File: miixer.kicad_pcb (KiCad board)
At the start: 2 copper layers, 60 x 30 mm, 8 parts, among them J1 USB_C_Receptacle_USB2.0_16P, U1 ESP32-C3-WROOM-02, U3 USBLC6-2SC6

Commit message: Update
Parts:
- added VR1: PTL60-15G1-103B2, 00_Luc:PTL6015G1103B2, F.Cu at (38.6, 110.0)
- added VR2: PTL60-15G1-103B2, 00_Luc:PTL6015G1103B2, F.Cu at (50.3, 110.0)
- added VR3: PTL60-15G1-103B2, 00_Luc:PTL6015G1103B2, F.Cu at (61.9, 110.0)
- added VR4: PTL60-15G1-103B2, 00_Luc:PTL6015G1103B2, F.Cu at (73.4, 110.0)
- R4, U1: moved to B.Cu
- moved R5 36.3 mm to (103.2, 32.5)
- moved J1 35.2 mm to (117.8, 37.0)
- moved R1 35.2 mm to (110.0, 37.7)
- moved R2 35.2 mm to (110.0, 35.9)
- moved U3 35.2 mm to (103.3, 36.7)
- moved R6 34.6 mm to (110.0, 32.5)
- moved R4 24.7 mm to (32.5, 44.2), turned to 180 degrees
- moved U1 19.3 mm to (37.7, 55.2), turned to -90 degrees
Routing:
- net /MCU/USB_D+: track 30.9 -> 0.97 mm
- net VBUS: track 2.83 -> 0.00 mm
- net +3.3V: track 0.00 -> 2.27 mm
- net /MCU/ENABLE: track 0.00 -> 2.25 mm
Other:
- board size 60 x 30 mm -> 90 x 90 mm

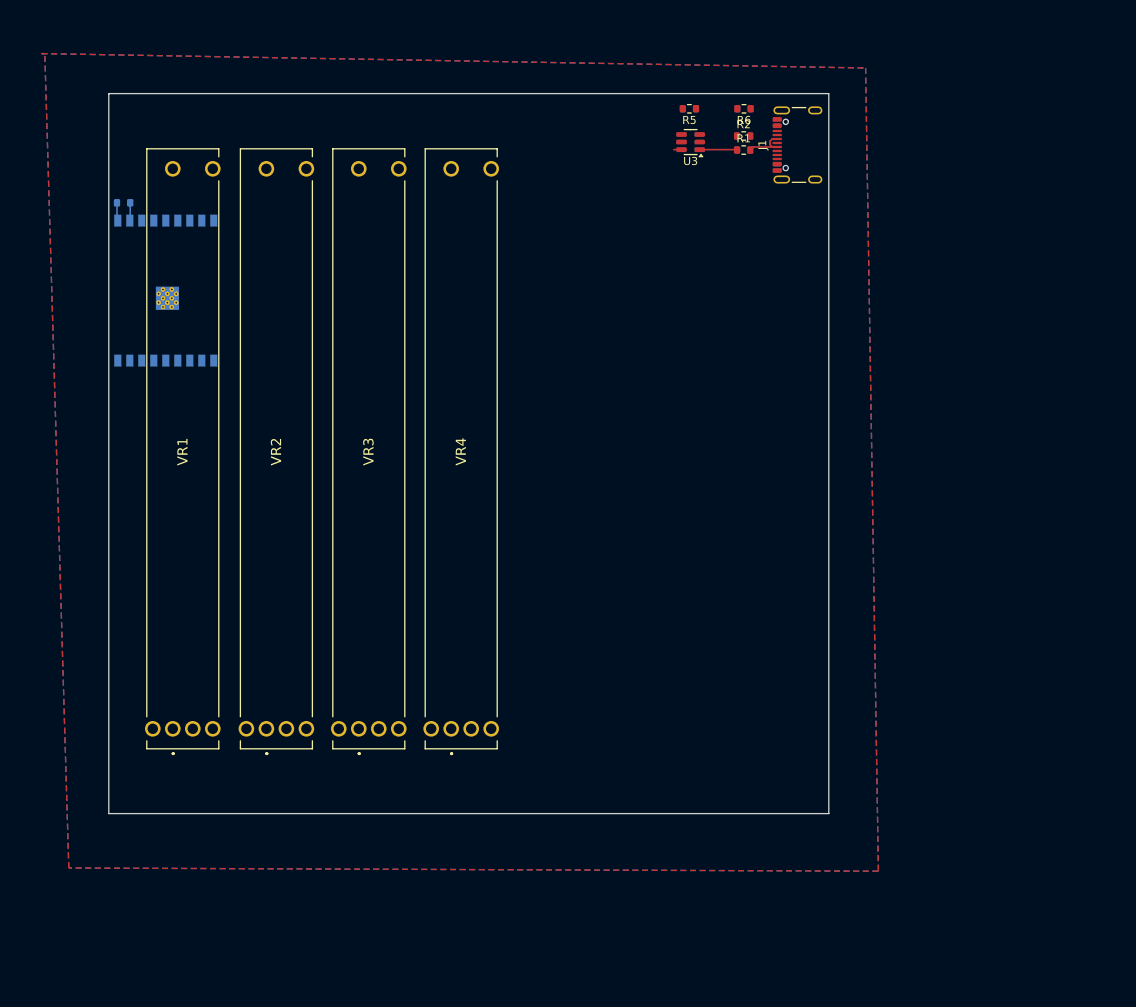
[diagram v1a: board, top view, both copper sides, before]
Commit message: Introduce buttons and update pcb layout
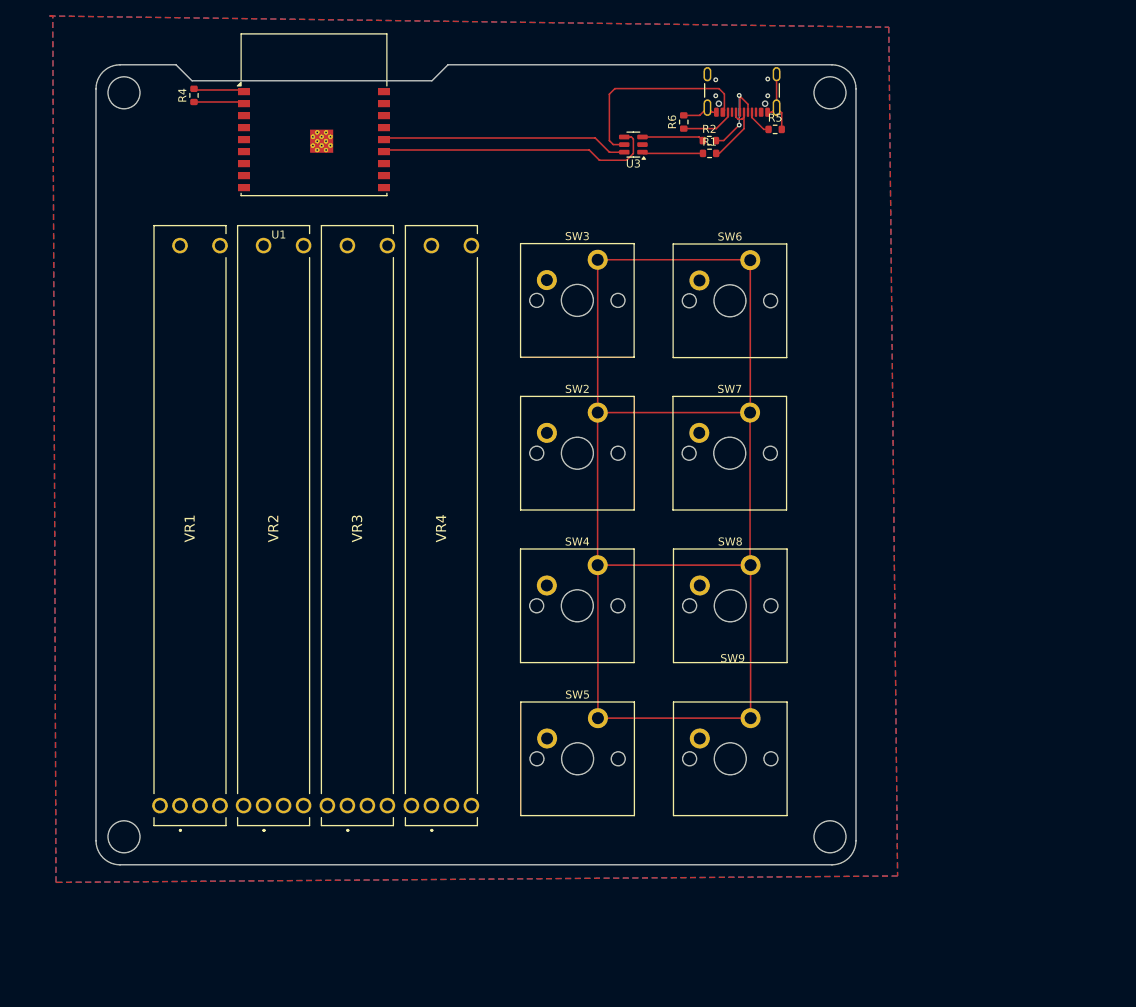
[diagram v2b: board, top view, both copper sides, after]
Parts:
- added SW2: SW_SPST, PCM_Switch_Keyboard_Cherry_MX:SW_Cherry_MX_PCB_1.00u, F.Cu at (89.2, 75.5)
- added SW3: SW_SPST, PCM_Switch_Keyboard_Cherry_MX:SW_Cherry_MX_PCB_1.00u, F.Cu at (89.2, 56.5)
- added SW4: SW_SPST, PCM_Switch_Keyboard_Cherry_MX:SW_Cherry_MX_PCB_1.00u, F.Cu at (89.2, 94.6)
- added SW5: SW_SPST, PCM_Switch_Keyboard_Cherry_MX:SW_Cherry_MX_PCB_1.00u, F.Cu at (89.2, 113.8)
- added SW6: SW_SPST, PCM_Switch_Keyboard_Cherry_MX:SW_Cherry_MX_PCB_1.00u, F.Cu at (108.2, 56.5)
- added SW7: SW_SPST, PCM_Switch_Keyboard_Cherry_MX:SW_Cherry_MX_PCB_1.00u, F.Cu at (108.2, 75.5)
- added SW8: SW_SPST, PCM_Switch_Keyboard_Cherry_MX:SW_Cherry_MX_PCB_1.00u, F.Cu at (108.3, 94.6)
- added SW9: SW_SPST, PCM_Switch_Keyboard_Cherry_MX:SW_Cherry_MX_PCB_1.00u, F.Cu at (108.3, 113.8)
- R4, U1: moved to F.Cu
- moved U1 26.4 mm to (56.2, 36.4), turned to 0 degrees
- moved R4 16.1 mm to (41.2, 30.8), turned to 90 degrees
- moved J1 11.2 mm to (109.8, 29.2), turned to 180 degrees
- moved R5 11.0 mm to (113.9, 35.1), turned to 0 degrees
- moved VR4 9.91 mm to (70.9, 119.6)
- moved VR3 9.71 mm to (60.4, 119.6)
- moved VR1 9.64 mm to (39.5, 119.6)
- moved VR2 9.61 mm to (50.0, 119.6)
- moved R6 7.71 mm to (102.5, 34.1), turned to 90 degrees
- moved U3 7.16 mm to (96.2, 37.0)
- moved R2 4.33 mm to (105.7, 36.5)
- moved R1 4.29 mm to (105.7, 38.1)
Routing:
- net GND: track 0.00 -> 204.2 mm, vias 0 -> 4
- net /MCU/USB_D-: track 0.00 -> 35.1 mm
- net /MCU/USB_D+: track 0.97 -> 30.8 mm
- net VBUS: track 0.00 -> 25.2 mm
- net /USB/USB_D-_RAW: track 0.00 -> 12.1 mm, vias 0 -> 2
- net /USB/USB_DN: track 0.00 -> 7.72 mm
- net /USB/CC2: track 0.00 -> 6.71 mm
- net +3.3V: track 2.27 -> 6.30 mm
- net /MCU/ENABLE: track 2.25 -> 6.24 mm
- net /USB/CC1: track 0.00 -> 3.35 mm
- net /USB/USB_D+_RAW: track 5.96 -> 9.26 mm
- net /USB/USB_DP: track 4.70 -> 7.62 mm
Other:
- board size 90 x 90 mm -> 95 x 100 mm

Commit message: Make square
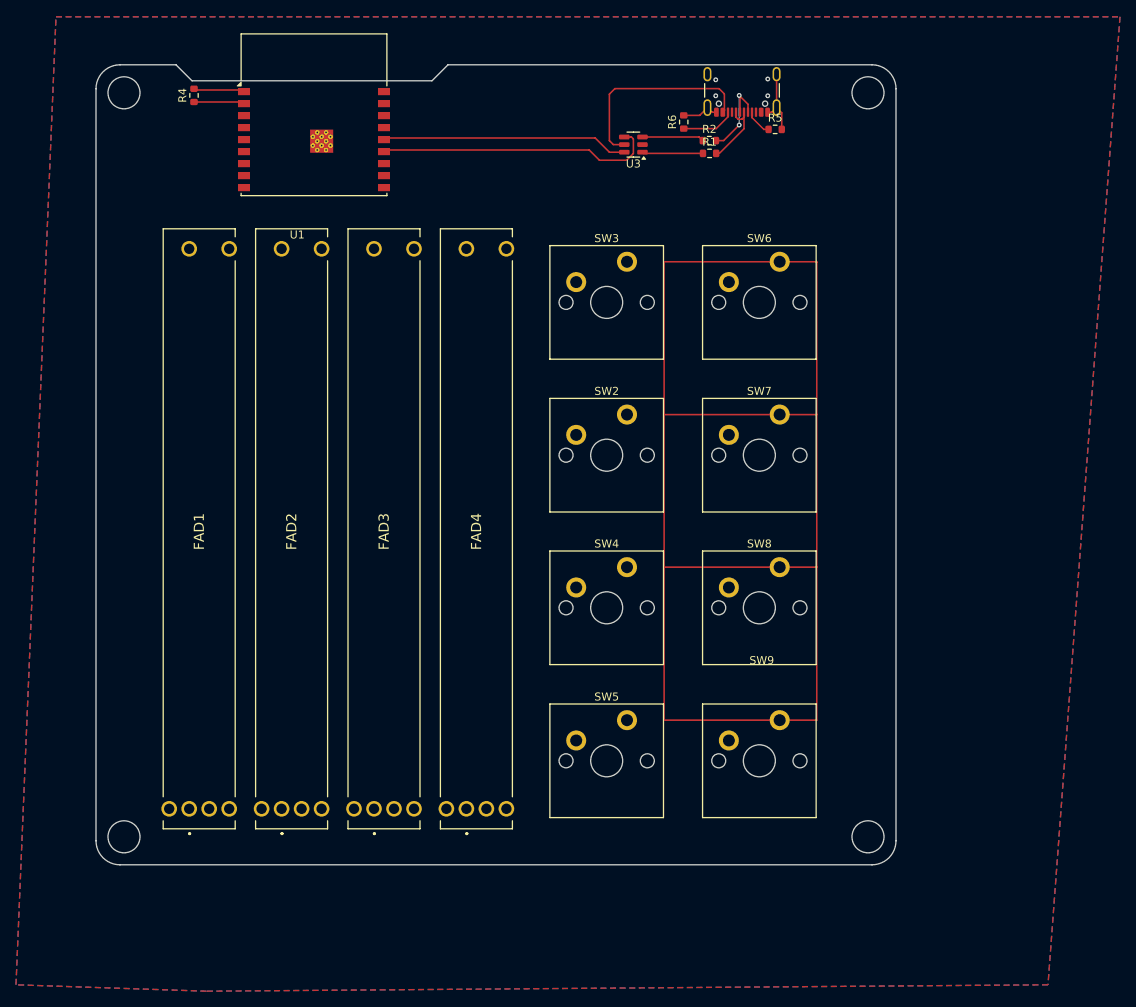
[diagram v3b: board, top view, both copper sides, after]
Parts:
- removed VR1, VR2, VR3, VR4: PTL60-15G1-103B2, 00_Luc:PTL6015G1103B2
- added FAD1: PTL60-15G1-103B2, 00_Luc:PTL6015G1103B2, F.Cu at (40.6, 120.0)
- added FAD2: PTL60-15G1-103B2, 00_Luc:PTL6015G1103B2, F.Cu at (52.2, 120.0)
- added FAD3: PTL60-15G1-103B2, 00_Luc:PTL6015G1103B2, F.Cu at (63.8, 120.0)
- added FAD4: PTL60-15G1-103B2, 00_Luc:PTL6015G1103B2, F.Cu at (75.3, 120.0)
- moved SW7 3.71 mm to (111.9, 75.8)
- moved SW6 3.68 mm to (111.9, 56.7)
- moved SW4 3.68 mm to (92.8, 94.9)
- moved SW3 3.67 mm to (92.8, 56.7)
- moved SW2 3.67 mm to (92.8, 75.8)
- moved SW8 3.64 mm to (111.9, 94.9)
- moved SW9 3.64 mm to (111.9, 114.0)
- moved SW5 3.64 mm to (92.8, 114.0)
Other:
- board size 95 x 100 mm -> 100 x 100 mm

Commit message: Add keys for each fader & update layout
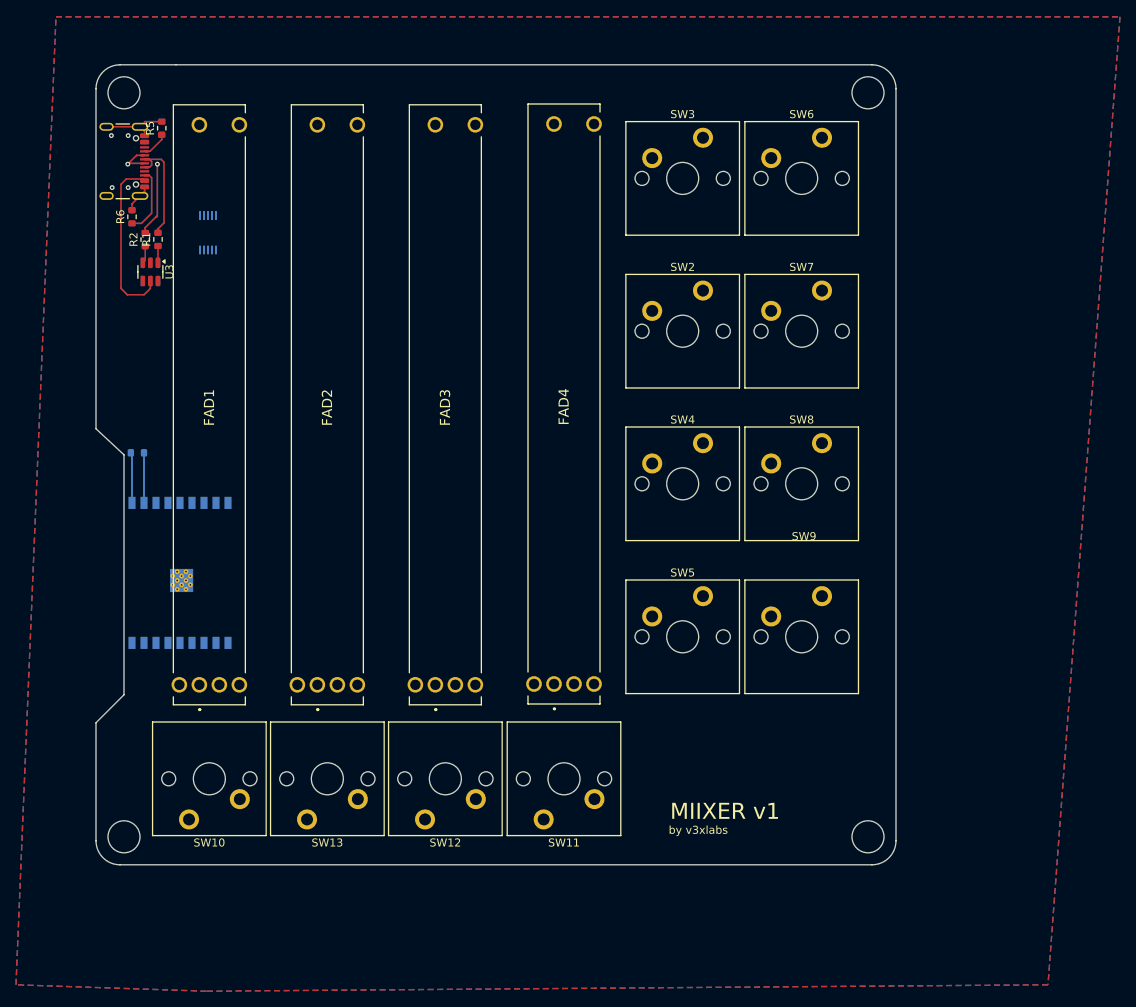
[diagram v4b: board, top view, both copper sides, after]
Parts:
- added SW10: SW_SPST, PCM_Switch_Keyboard_Cherry_MX:SW_Cherry_MX_PCB_1.00u, F.Cu at (43.2, 116.2)
- added SW11: SW_SPST, PCM_Switch_Keyboard_Cherry_MX:SW_Cherry_MX_PCB_1.00u, F.Cu at (87.5, 116.2)
- added SW12: SW_SPST, PCM_Switch_Keyboard_Cherry_MX:SW_Cherry_MX_PCB_1.00u, F.Cu at (72.7, 116.2)
- added SW13: SW_SPST, PCM_Switch_Keyboard_Cherry_MX:SW_Cherry_MX_PCB_1.00u, F.Cu at (57.9, 116.2)
- added U2: ADS1115IDGS, Package_SO:TSSOP-10_3x3mm_P0.5mm, B.Cu at (43.0, 48.0)
- R4, U1: moved to B.Cu
- moved J1 79.0 mm to (31.4, 39.1), turned to -90 degrees
- moved R5 76.7 mm to (37.2, 34.9), turned to 90 degrees
- moved R2 71.6 mm to (35.1, 48.9), turned to 90 degrees
- moved R6 70.0 mm to (33.5, 46.0)
- moved R1 69.8 mm to (36.8, 48.8), turned to 90 degrees
- moved U3 62.4 mm to (35.8, 52.9), turned to -90 degrees
- moved U1 56.7 mm to (39.5, 90.5), turned to -90 degrees
- moved R4 45.2 mm to (34.2, 75.5), turned to 180 degrees
- moved FAD4 19.1 mm to (86.2, 104.4)
- moved SW2 18.2 mm to (102.3, 60.3)
- moved SW3 18.2 mm to (102.3, 41.2)
- moved SW4 18.2 mm to (102.3, 79.4)
- moved SW5 18.2 mm to (102.3, 98.5)
- moved FAD3 17.3 mm to (71.4, 104.5)
- moved SW6 16.4 mm to (117.2, 41.2)
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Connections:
- FAD1 pad 1: unconnected-(FAD1-CCW-Pad1) -> Net-(FAD1-CCW)
- FAD1 pad B1: unconnected-(FAD1-B_(+)-PadB1) -> Net-(FAD1-B_(+))
- FAD1 pad E1: unconnected-(FAD1-E_(-)-PadE1) -> GND
- FAD2 pad 1: unconnected-(FAD2-CCW-Pad1) -> Net-(FAD2-CCW)
- FAD2 pad B1: unconnected-(FAD2-B_(+)-PadB1) -> Net-(FAD2-B_(+))
- FAD2 pad E1: unconnected-(FAD2-E_(-)-PadE1) -> GND
- FAD3 pad 1: unconnected-(FAD3-CCW-Pad1) -> Net-(FAD3-CCW)
- FAD3 pad B1: unconnected-(FAD3-B_(+)-PadB1) -> Net-(FAD3-B_(+))
- FAD3 pad E1: unconnected-(FAD3-E_(-)-PadE1) -> GND
- FAD4 pad 1: unconnected-(FAD4-CCW-Pad1) -> Net-(FAD4-CCW)
- FAD4 pad B1: unconnected-(FAD4-B_(+)-PadB1) -> Net-(FAD4-B_(+))
- FAD4 pad E1: unconnected-(FAD4-E_(-)-PadE1) -> GND
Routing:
- net GND: track 204.2 -> 12.1 mm
- net /MCU/USB_D-: track 35.1 -> 0.00 mm
- net /MCU/USB_D+: track 30.8 -> 0.00 mm
- net /USB/USB_DN: track 7.72 -> 2.20 mm
- net /USB/USB_DP: track 7.62 -> 2.10 mm
- net /USB/USB_D+_RAW: track 9.26 -> 14.1 mm
- net VBUS: track 25.2 -> 21.6 mm
- net /USB/CC2: track 6.71 -> 8.98 mm
- net /USB/USB_D-_RAW: track 12.1 -> 14.0 mm
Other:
- outline, holes or cut-outs redrawn

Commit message: Reorg layout and remove fader keys
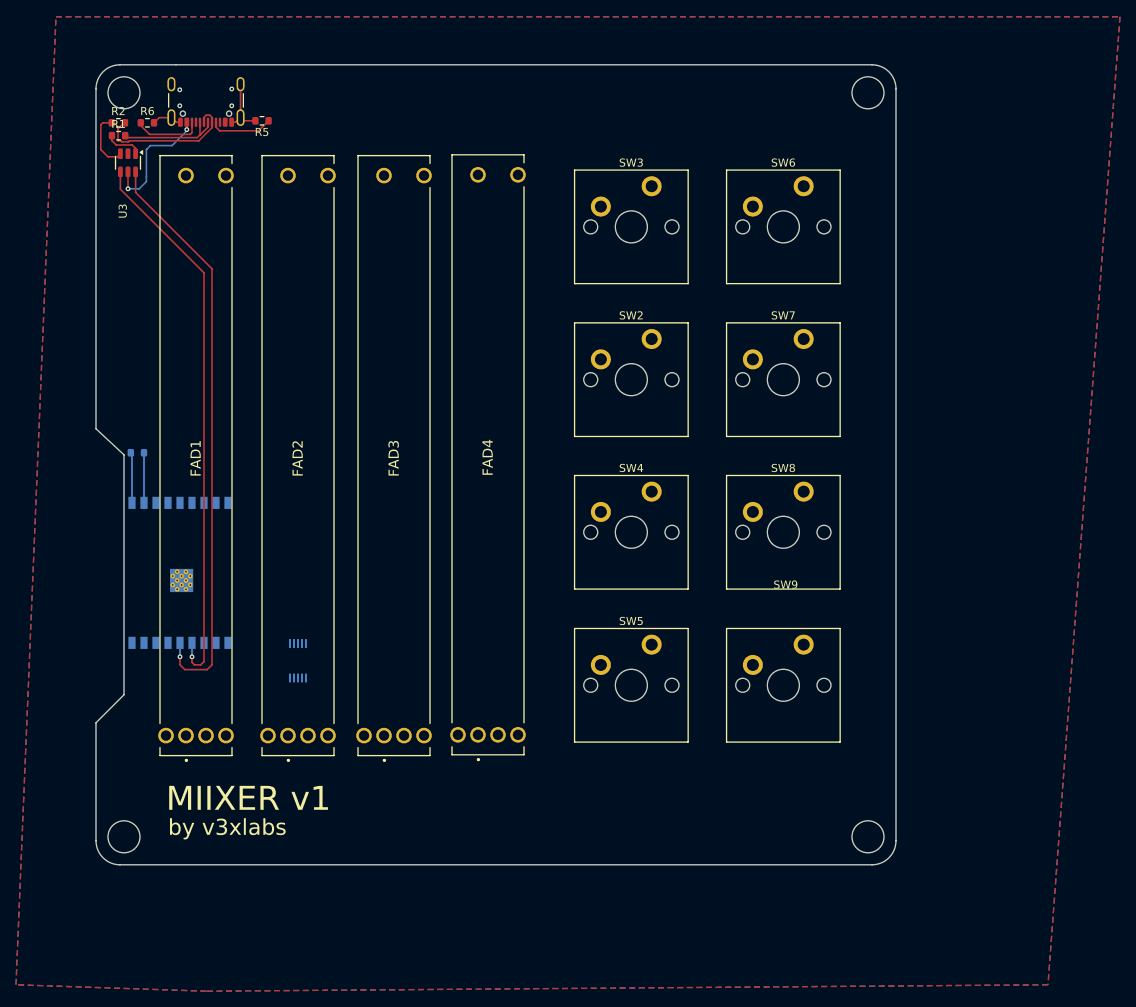
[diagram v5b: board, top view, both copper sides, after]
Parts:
- removed SW10, SW11, SW12, SW13: SW_SPST, PCM_Switch_Keyboard_Cherry_MX:SW_Cherry_MX_PCB_1.00u
- moved U2 54.7 mm to (54.2, 101.5)
- moved R2 15.0 mm to (31.8, 34.3), turned to 0 degrees
- moved J1 14.2 mm to (42.8, 30.5), turned to 180 degrees
- moved U3 13.9 mm to (33.0, 39.2)
- moved R1 13.9 mm to (31.8, 35.9), turned to 0 degrees
- moved R5 12.6 mm to (49.8, 34.0), turned to 180 degrees
- moved R6 11.9 mm to (35.4, 34.2), turned to 0 degrees
- moved FAD4 11.4 mm to (76.8, 110.8)
- moved FAD3 9.03 mm to (65.0, 110.8)
- moved SW2 8.82 mm to (95.9, 66.4)
- moved SW4 8.82 mm to (95.9, 85.4)
- moved SW5 8.82 mm to (95.9, 104.6)
- moved SW3 8.82 mm to (95.9, 47.3)
- moved FAD2 7.33 mm to (53.0, 110.8)
- moved FAD1 6.57 mm to (40.2, 110.8)
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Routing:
- net /MCU/USB_D+: track 0.00 -> 72.8 mm, vias 0 -> 1
- net /MCU/USB_D-: track 0.00 -> 69.8 mm, vias 0 -> 1
- net VBUS: track 21.6 -> 16.2 mm, vias 0 -> 2
- net /USB/USB_DN: track 2.20 -> 7.55 mm
- net /USB/CC1: track 3.35 -> 7.89 mm
- net /USB/USB_D-_RAW: track 14.0 -> 18.3 mm, vias 2 -> 0
- net /USB/USB_DP: track 2.10 -> 4.68 mm
- net /USB/USB_D+_RAW: track 14.1 -> 13.2 mm
- net GND: track 12.1 -> 11.4 mm
